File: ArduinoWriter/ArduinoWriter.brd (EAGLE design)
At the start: 68.5 x 53.5 mm, 11 parts, among them IC1 ATMEGA328-PU, IC2 TC74HC08AP, Q1 HUSG-16.000-20, SW1 SS-12D01-VG4, U1 ARRDUINOUNO-NOSILK

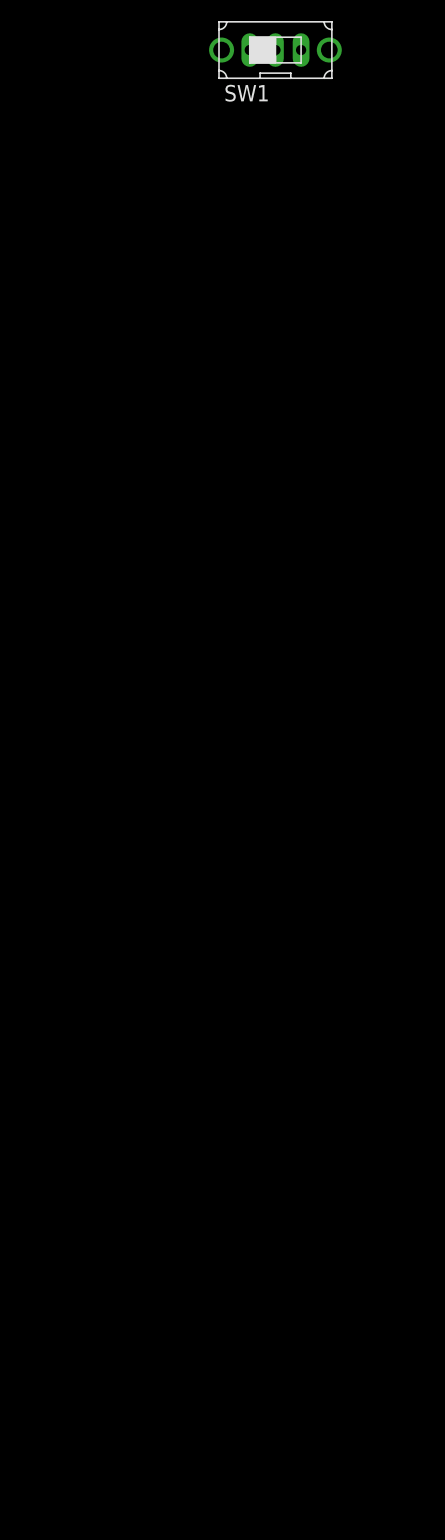
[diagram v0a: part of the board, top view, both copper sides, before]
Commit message: SEWR_ICSP 切替回路実装
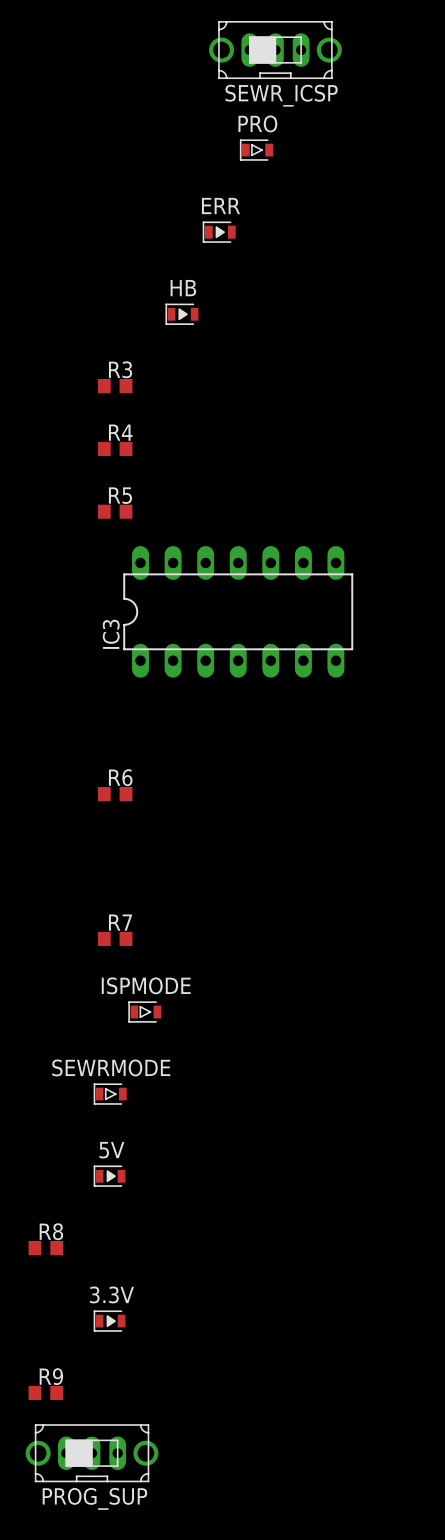
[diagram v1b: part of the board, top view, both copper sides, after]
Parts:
- added 3.3V, 5V: OSBL1608C1A, LED:LEDC1608X39N_B
- added ERR, HB: OSHR1608C1A, LED:LEDC1608X39N_R
- added IC3: TC74HC32AP, 東芝_74LSシリーズ:DIL14
- added ISPMODE, PRO, SEWRMODE: OSTG1608C1A, LED:LEDC1608X39N_G
- added PROG_SUP: SS-12D01-VG4, スライドスイッチ:SS-12D01-VG4
- added R3, R4, R5, R6, R7, R8, R9: 1k, RCL:R0603
- renumbered SW1 to SEWR_ICSP
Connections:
- removed net RX1: SEPR.1
- removed net TX1: SEPR.3
- new net ERROR: IC1.14, R4.2
- new net HEARTBEAT: IC1.15, R5.2
- new net N$5: HB.1, R5.1
- new net N$6: ISPMODE.A, R6.1
- new net N$7: R7.1, SEWRMODE.A
- new net N$8: 5V.1, R8.1
- new net N$9: 3.3V.1, R9.1
- new net PCRX_ICTX: IC2.2, IC2.5, U1.1
- new net PROGRAMMING: IC1.13, R3.2
- new net PROG_SUPPLY: ICSP.2, PROG_SUP.NO, SEPR.2
- new net SE_TX: IC2.6, SEPR.3
- new net WRITER_TX: IC1.3, IC2.3
- net +3.3V: now also R9.2
- net +5V: now also PROG_SUP.COM, R8.2; no longer ICSP.2, SEPR.2
- net GND: now also 3.3V.2, 5V.2, ERR.2, HB.2, IC3.7, ISPMODE.K, PRO.K, SEWRMODE.K
- net ICSP_RESET: now also IC1.16
- net MISO: now also IC1.18
- net MOSI: now also IC1.17
- net N$3: now also PRO.A, R3.1; no longer IC1.2, U1.0
- net N$4: now also ERR.1, R4.1; no longer IC1.3, U1.1
- net PCTX_ICRX: now also U1.0
- net RESET_SIG: now also IC3.2, IC3.5; no longer IC2.2, IC2.5
- net SCK: now also IC1.19
- net SE_RESET: now also IC3.3; no longer IC2.6
- net SE_RX: now also SEPR.1
- net SE_SW: now also IC3.4, R7.2
- net VCC: now also IC3.14
- net WRITER_RESET: now also IC3.6; no longer IC2.3
- net WRITER_RX: now also IC1.2
- net WR_SW: now also IC3.1, R6.2

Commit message: レイアウト完了
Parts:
- added 5V_OUT: OSBL1608C1A, LED:LEDC1608X39N_B
- added C3, C4: 10u, RCL:C0805
- added R10, R11, R12: 1k, RCL:R0603
- added RX_LED, TX_LED: OSTG1608C1A, LED:LEDC1608X39N_G
- added T1, T2: IRLML6344TRPBF, FET:SOT95P240X110-3N
- moved R9 201.3 mm to (14.0, 41.5)
- moved 3.3V 194.7 mm to (10.0, 41.5), turned to 180 degrees
- moved R8 192.6 mm to (14.0, 44.0)
- moved 5V 185.9 mm to (10.0, 44.0), turned to 180 degrees
- moved PROG_SUP 181.4 mm to (22.0, 16.0), turned to 270 degrees
- moved SEWRMODE 166.8 mm to (54.0, 20.0), turned to 90 degrees
- moved R7 152.3 mm to (54.0, 16.5), turned to 270 degrees
- moved ISPMODE 151.5 mm to (54.0, 11.0), turned to 90 degrees
- moved IC3 141.2 mm to (26.0, 42.0), turned to 180 degrees
- moved R6 134.0 mm to (54.0, 7.50), turned to 270 degrees
- moved R5 127.6 mm to (14.0, 36.5)
- moved R4 120.4 mm to (14.0, 34.0)
- moved R3 113.1 mm to (14.0, 31.5)
- moved HB 111.1 mm to (10.0, 36.5), turned to 180 degrees
- moved ERR 101.9 mm to (10.0, 34.0), turned to 180 degrees
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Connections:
- removed net VCC: IC2.14, IC3.14
- new net N$10: 5V_OUT.1, R10.1
- new net N$11: RX_LED.K, T1.3
- new net N$12: T2.3, TX_LED.K
- new net N$13: R11.1, RX_LED.A
- new net N$14: R12.1, TX_LED.A
- new net SE_SW_LED: IC3.8, R7.2
- new net WR_SW_LED: IC3.11, R6.2
- net +5V: now also C3.1, C4.1, IC2.14, IC3.14, R11.2, R12.2
- net GND: now also 5V_OUT.2, C3.2, C4.2, IC3.10, IC3.13, T1.2, T2.2
- net PCRX_ICTX: now also T1.1
- net PCTX_ICRX: now also T2.1
- net PROG_SUPPLY: now also R10.2
- net SE_SW: now also IC3.9; no longer R7.2
- net WR_SW: now also IC3.12; no longer R6.2

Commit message: 配線・シルク完
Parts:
- added POWER: (no value), pinhead:1X03
- added RESET: TS-06104, タクトスイッチ:TS-06104
- moved 3.3V 21.5 mm to (10.0, 20.0)
- moved 5V 21.5 mm to (10.0, 22.5)
- moved R8 21.5 mm to (14.0, 22.5)
- moved R9 21.5 mm to (14.0, 20.0)
- moved R11 18.5 mm to (14.0, 39.0)
- moved R12 18.5 mm to (14.0, 41.5)
- moved RX_LED 18.5 mm to (10.0, 39.0)
- moved T1 18.5 mm to (10.0, 45.5)
- moved T2 18.5 mm to (14.0, 45.5)
- moved TX_LED 18.5 mm to (10.0, 41.5)
- moved 5V_OUT 9.39 mm to (18.5, 10.0)
- moved R10 8.94 mm to (22.0, 10.0), turned to 0 degrees
- moved R6 4.66 mm to (58.5, 6.30), turned to 0 degrees
- moved R7 4.06 mm to (58.0, 15.8), turned to 0 degrees
- moved R2 3.73 mm to (34.7, 22.5), turned to 180 degrees
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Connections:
- net +3.3V: now also POWER.2
- net +5V: now also POWER.1
- net GND: now also POWER.3, RESET.B1, RESET.B2
- net RESET_SIG: now also RESET.A1, RESET.A2
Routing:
- net +5V: track 0.00 -> 154.1 mm, vias 0 -> 2
- net RESET_SIG: track 0.00 -> 105.4 mm
- net SE_SW: track 0.00 -> 84.4 mm, vias 0 -> 2
- net WR_SW_LED: track 0.00 -> 77.8 mm, vias 0 -> 4
- net PCTX_ICRX: track 0.00 -> 76.4 mm, vias 0 -> 2
- net WR_SW: track 0.00 -> 74.5 mm
- net SE_SW_LED: track 0.00 -> 72.2 mm, vias 0 -> 5
- net PCRX_ICTX: track 0.00 -> 67.5 mm
- net +3.3V: track 0.00 -> 66.0 mm, vias 0 -> 2
- net SE_RESET: track 0.00 -> 59.8 mm, vias 0 -> 2
- net PROG_SUPPLY: track 0.00 -> 58.2 mm
- net SCK: track 0.00 -> 44.4 mm
- net WRITER_TX: track 0.00 -> 43.3 mm, vias 0 -> 1
- net HEARTBEAT: track 0.00 -> 43.1 mm
- net SE_TX: track 0.00 -> 43.1 mm, vias 0 -> 1
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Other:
- board size 68.5 x 53.5 mm -> 68.5 x 55 mm
- board text added: "0V"
- board text added: "0V | 3.3V | 5V"
- board text added: "2022/02/01 V1.0 Designed by Bigstone"
- board text added: "5V"
- board text added: "Arduino Writer"
- board text added: "ICSP"
- board text added: "MISO"
- board text added: "MOSI"
- board text added: "NC"
- board text added: "POWER"
- board text added: "RES"
- board text added: "RX"
- board text added: "SCK"
- board text added: "SEWR"
- board text added: "SE_WR"
- board text added: "TX"

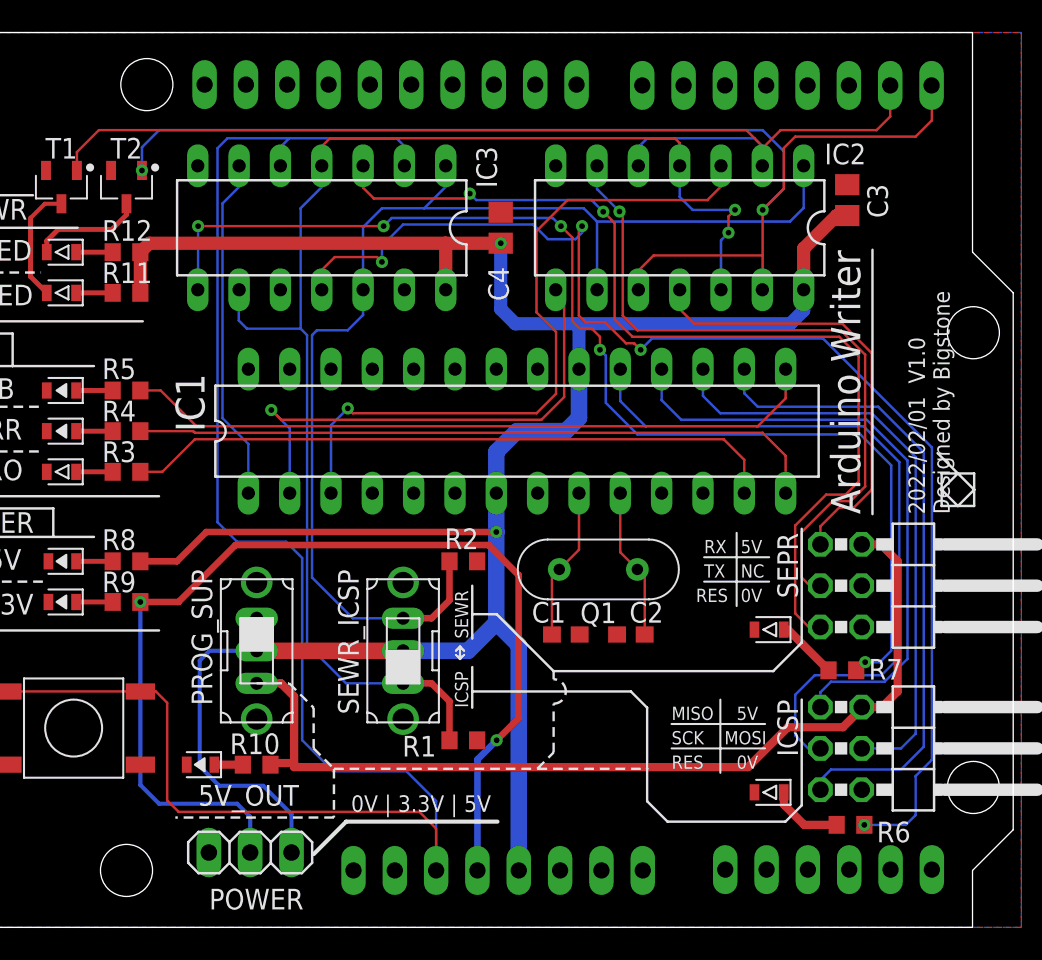
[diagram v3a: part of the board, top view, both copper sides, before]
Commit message: RXTX欠陥部修正
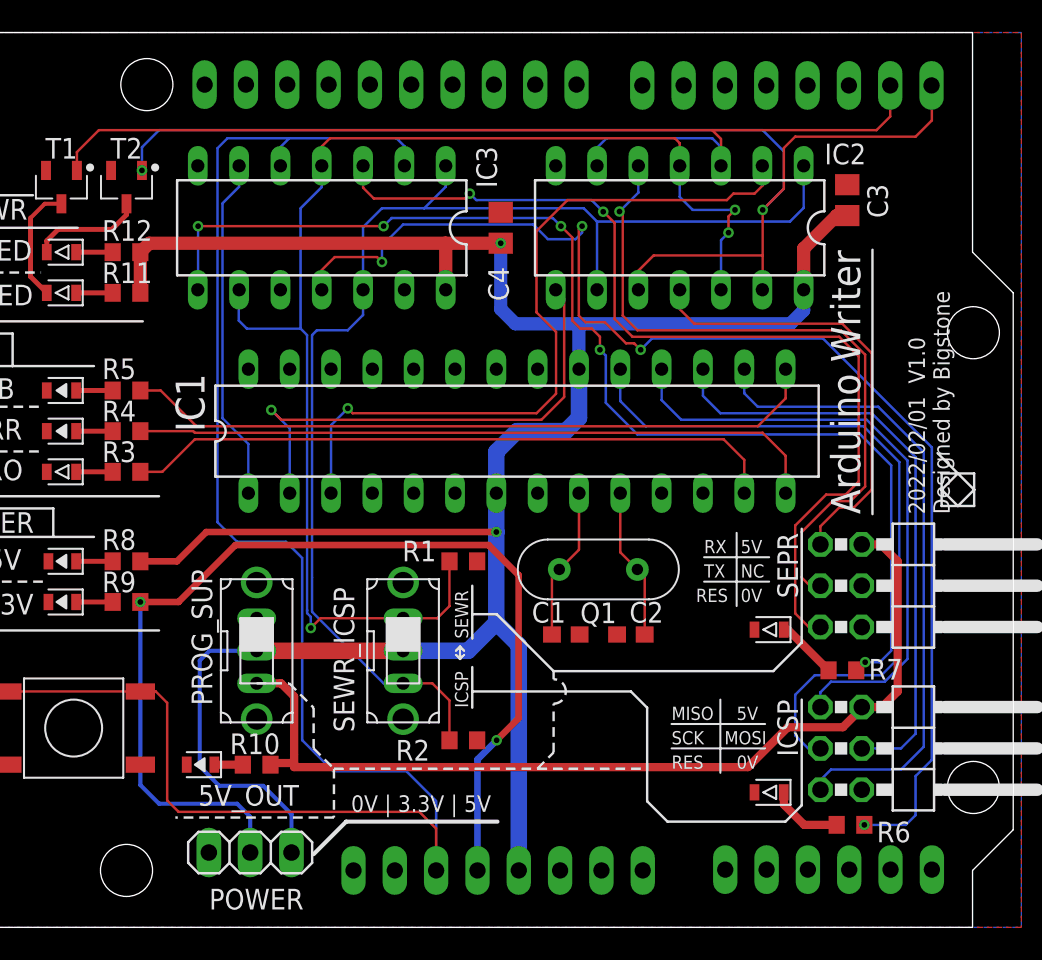
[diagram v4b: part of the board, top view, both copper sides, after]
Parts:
- moved R1 11.0 mm to (34.7, 22.5)
- moved R2 11.0 mm to (34.7, 11.5)
- turned SEWR_ICSP to 270 degrees
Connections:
- net PCRX_ICTX: now also IC2.3, IC2.6; no longer IC2.2, IC2.5
- net SE_TX: now also IC2.5; no longer IC2.6
- net WRITER_TX: now also IC2.2; no longer IC2.3
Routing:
- net WR_SW: track 74.5 -> 77.4 mm
- net WRITER_TX: track 43.3 -> 45.8 mm
- net SE_SW: track 84.4 -> 82.9 mm, vias 2 -> 3
- net PCRX_ICTX: track 67.5 -> 66.7 mm

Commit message: スイッチ・一部表示変更
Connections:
- net PROG_SUPPLY: now also SEPR.4
- net SE_RX: now also SEPR.3; no longer SEPR.1
- net SE_TX: now also SEPR.1; no longer SEPR.3
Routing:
- net SE_TX: track 43.0 -> 39.1 mm
- net SE_RX: track 27.7 -> 29.7 mm
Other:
- board text added: "2022/02/01 V1.1 Designed by Bigstone"
- board text added: "IRX"
- board text added: "ITX"
- board text removed: "2022/02/01 V1.0 Designed by Bigstone"
- board text removed: "NC"
- board text removed: "RX"
- board text removed: "TX"
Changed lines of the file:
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@@
 <drawing>
 <settings>
-<setting alwaysvectorfont="no"/>
+<setting alwaysvectorfont="yes"/>
 <setting verticaltext="up"/>
 </settings>
@@
 <wire x1="47.5" y1="11" x2="53.25" y2="11" width="0.127" layer="21"/>
 <text x="51.75" y="23" size="0.8128" layer="21">5V</text>
-<text x="51.75" y="21.5" size="0.8128" layer="21">NC</text>
 <text x="51.75" y="20" size="0.8128" layer="21">0V</text>
 <text x="49" y="20" size="0.8128" layer="21">RES</text>
-<text x="49.5" y="21.5" size="0.8128" layer="21">TX</text>
-<text x="49.5" y="23" size="0.8128" layer="21">RX</text>
+<text x="49.3" y="21.5" size="0.8128" layer="21">ITX</text>
+<text x="49.3" y="23" size="0.8128" layer="21">IRX</text>
 <text x="51.5" y="12.75" size="0.8128" layer="21">5V</text>
 <text x="51.5" y="9.75" size="0.8128" layer="21">0V</text>
@@
 <wire x1="9.5" y1="25.75" x2="9.5" y2="24" width="0.15" layer="21"/>
 <text x="59.1" y="25.4" size="1.8" layer="21" rot="R90">Arduino Writer</text>
-<text x="64.6" y="25.4" size="1.016" layer="21" rot="R90">2022/02/01  V1.0
+<text x="64.6" y="25.4" size="1.016" layer="21" rot="R90">2022/02/01  V1.1
 Designed by Bigstone
 </text>
@@
 <wire x1="27.5" y1="6.5" x2="36.8" y2="6.5" width="0.254" layer="21"/>
 <text x="27.8" y="7.1" size="1.016" layer="21">0V | 3.3V | 5V</text>
+<wire x1="49.2" y1="23.4" x2="48.1" y2="23.4" width="0.127" layer="21"/>
+<wire x1="49.2" y1="23.4" x2="48.8" y2="23" width="0.127" layer="21"/>
+<wire x1="48.8" y1="23.8" x2="49.2" y2="23.4" width="0.127" layer="21"/>
+<wire x1="49.2" y1="21.9" x2="48.1" y2="21.9" width="0.127" layer="21"/>
+<wire x1="48.1" y1="21.9" x2="48.5" y2="21.5" width="0.127" layer="21"/>
+<wire x1="48.1" y1="21.9" x2="48.5" y2="22.3" width="0.127" layer="21"/>
+<text x="51.75" y="21.5" size="0.8128" layer="21">0V</text>
 </plain>
 <attributes>
@@
 <signal name="SE_RX">
 <contactref element="IC2" pad="11"/>
-<contactref element="SEPR" pad="1"/>
 <wire x1="48" y1="39.19" x2="48" y2="38.0048" width="0.1524" layer="1"/>
 <wire x1="48" y1="38.0048" x2="48.9" y2="37.1048" width="0.1524" layer="1"/>
 <wire x1="48.9" y1="37.1048" x2="57.9952" y2="37.1048" width="0.1524" layer="1"/>
-<wire x1="59.8" y1="26.9" x2="58.7" y2="25.8" width="0.1524" layer="1"/>
-<wire x1="58.7" y1="25.8" x2="57.8" y2="25.8" width="0.1524" layer="1"/>
-<wire x1="56.65" y1="24.65" x2="56.65" y2="23.54" width="0.1524" layer="1"/>
 <wire x1="57.9952" y1="37.1048" x2="59.8" y2="35.3" width="0.1524" layer="1"/>
 <wire x1="59.8" y1="35.3" x2="59.8" y2="26.9" width="0.1524" layer="1"/>
-<wire x1="57.8" y1="25.8" x2="56.65" y2="24.65" width="0.1524" layer="1"/>
+<contactref element="SEPR" pad="3"/>
+<wire x1="59.8" y1="26.9" x2="58" y2="25.1" width="0.15" layer="1"/>
+<wire x1="58" y1="22.35" x2="56.65" y2="21" width="0.15" layer="1"/>
+<wire x1="58" y1="25.1" x2="58" y2="22.35" width="0.15" layer="1"/>
 </signal>
 <signal name="PCTX_ICRX">
@@
 </signal>
 <signal name="SE_TX">
-<contactref element="SEPR" pad="3"/>
 <via x="44.3" y="44" extent="1-16" drill="0.35"/>
 <wire x1="44.3" y1="44" x2="44.5" y2="43.8" width="0.1524" layer="1"/>
 <wire x1="44.5" y1="43.8" x2="44.5" y2="37.6" width="0.1524" layer="1"/>
 <wire x1="44.5" y1="37.6" x2="45.4" y2="36.7" width="0.1524" layer="1"/>
-<wire x1="57.4" y1="26.2" x2="55.5" y2="24.3" width="0.1524" layer="1"/>
-<wire x1="55.5" y1="24.3" x2="55.5" y2="21.5" width="0.1524" layer="1"/>
-<wire x1="55.5" y1="21.5" x2="56" y2="21" width="0.1524" layer="1"/>
-<wire x1="56" y1="21" x2="56.65" y2="21" width="0.1524" layer="1"/>
 <wire x1="45.4" y1="36.7" x2="57.9" y2="36.7" width="0.1524" layer="1"/>
 <wire x1="57.9" y1="36.7" x2="59.4" y2="35.2" width="0.1524" layer="1"/>
@@
 <wire x1="44.3" y1="44" x2="45.46" y2="45.16" width="0.1524" layer="16"/>
 <wire x1="45.46" y1="45.16" x2="45.46" y2="46.81" width="0.1524" layer="16"/>
+<contactref element="SEPR" pad="1"/>
+<wire x1="57.4" y1="26.2" x2="56.65" y2="25.45" width="0.15" layer="1"/>
+<wire x1="56.65" y1="25.45" x2="56.65" y2="23.54" width="0.15" layer="1"/>
 </signal>
 <signal name="HEARTBEAT">
@@
 <wire x1="24.3" y1="10.1" x2="24.3" y2="9.85" width="0.508" layer="1"/>
 <wire x1="24.3" y1="10.6" x2="24.3" y2="10.1" width="0.508" layer="1"/>
+<contactref element="SEPR" pad="4"/>
+<wire x1="59.19" y1="23.54" x2="59.19" y2="21" width="0" layer="19" extent="1-1"/>
 </signal>
 <signal name="N$10">
